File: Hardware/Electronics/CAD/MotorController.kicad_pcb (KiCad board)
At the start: 2 copper layers, 42.3 x 42.3 mm, 17 parts, among them J1 MPE 094-1-006, J2 CONN_01X03, J3 SolderTerminal, J5 CONN_01X04, SW2 Taster 9314, U1 LD1117S33CTR, U2 MAX471, U3 TMC2130, U4 ESP-12E, U5 HiLink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

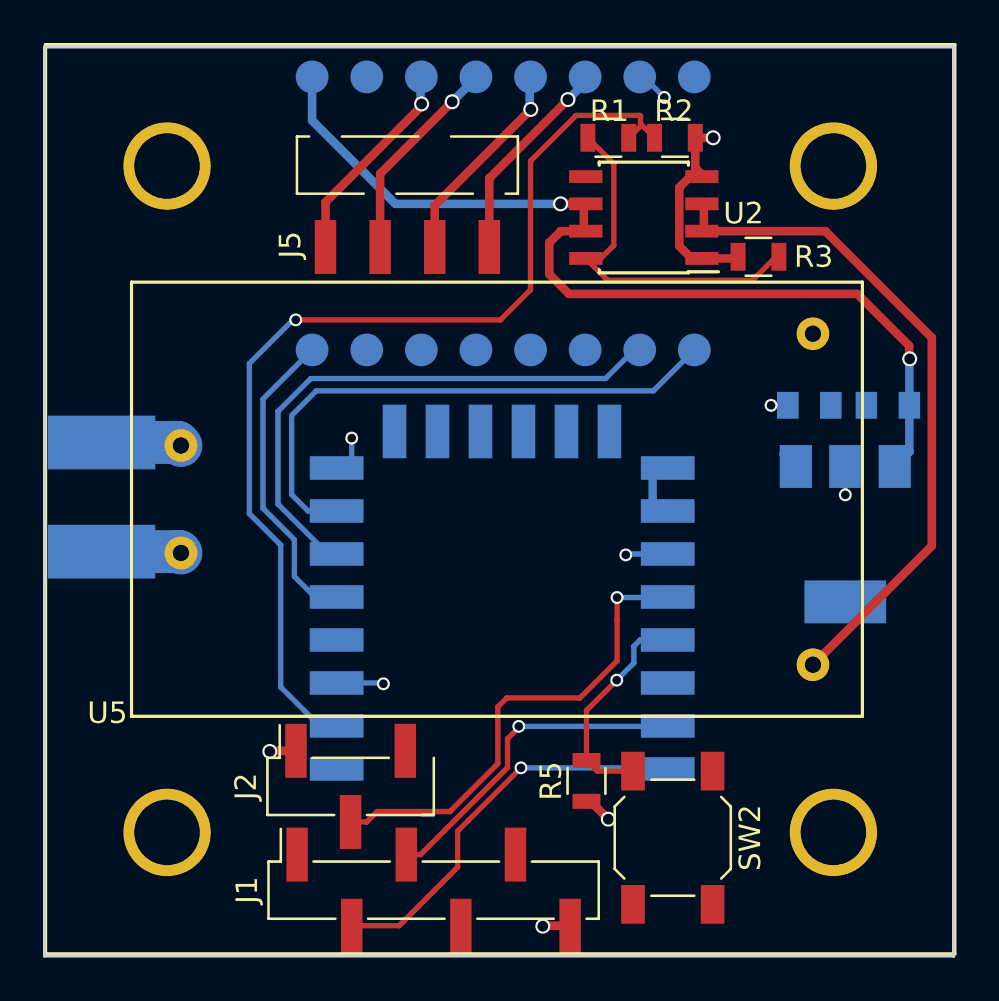
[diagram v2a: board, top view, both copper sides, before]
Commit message: part reference cleanup
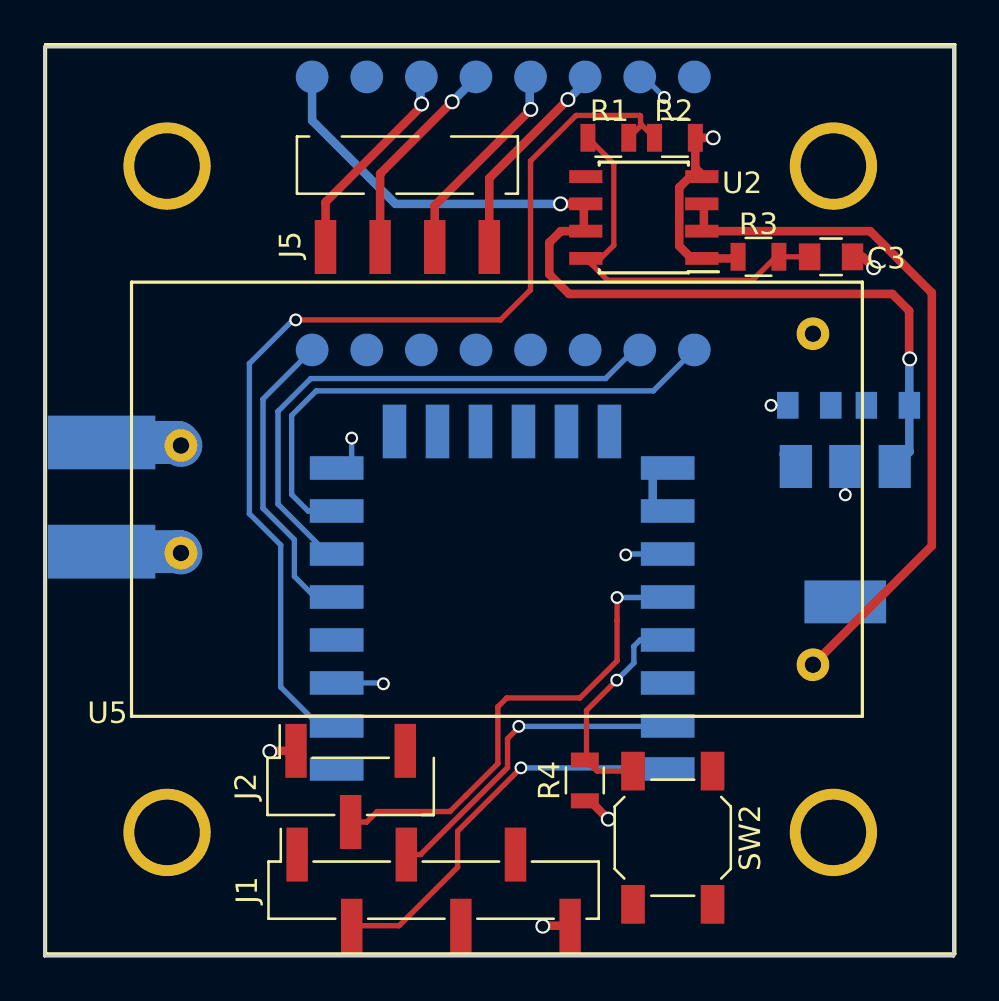
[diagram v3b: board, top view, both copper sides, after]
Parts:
- removed R5: RND 0805 1 10K, Resistors_SMD:R_0805
- added C3: 0805 47uF, Capacitors_SMD:C_0805, F.Cu at (212.5, 47.0)
- added R4: RND 0805 1 10K, Resistors_SMD:R_0805, F.Cu at (201.1, 71.4)
- C1, C2: value C -> 0805 10uF
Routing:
- net Net-(C3-Pad2): track 17.7 -> 19.1 mm
- net Net-(U2-Pad2): track 31.4 -> 32.7 mm
- net GND: track 16.8 -> 18.0 mm, vias 4 -> 5
- net +12V: track 45.2 -> 46.1 mm

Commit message: library linkage fix
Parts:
- SW2: value Taster 9314 -> SMD 4x4mm Button
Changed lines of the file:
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@@
       (effects (font (size 1 1) (thickness 0.15)))
     )
-    (fp_text value "Taster 9314" (at 0 3.7 270) (layer F.Fab)
+    (fp_text value "SMD 4x4mm Button" (at 0 3.7 270) (layer F.Fab)
       (effects (font (size 1 1) (thickness 0.15)))
     )
